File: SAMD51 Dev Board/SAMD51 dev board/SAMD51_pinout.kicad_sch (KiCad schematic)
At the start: 10 parts, among them U1 SAMD51

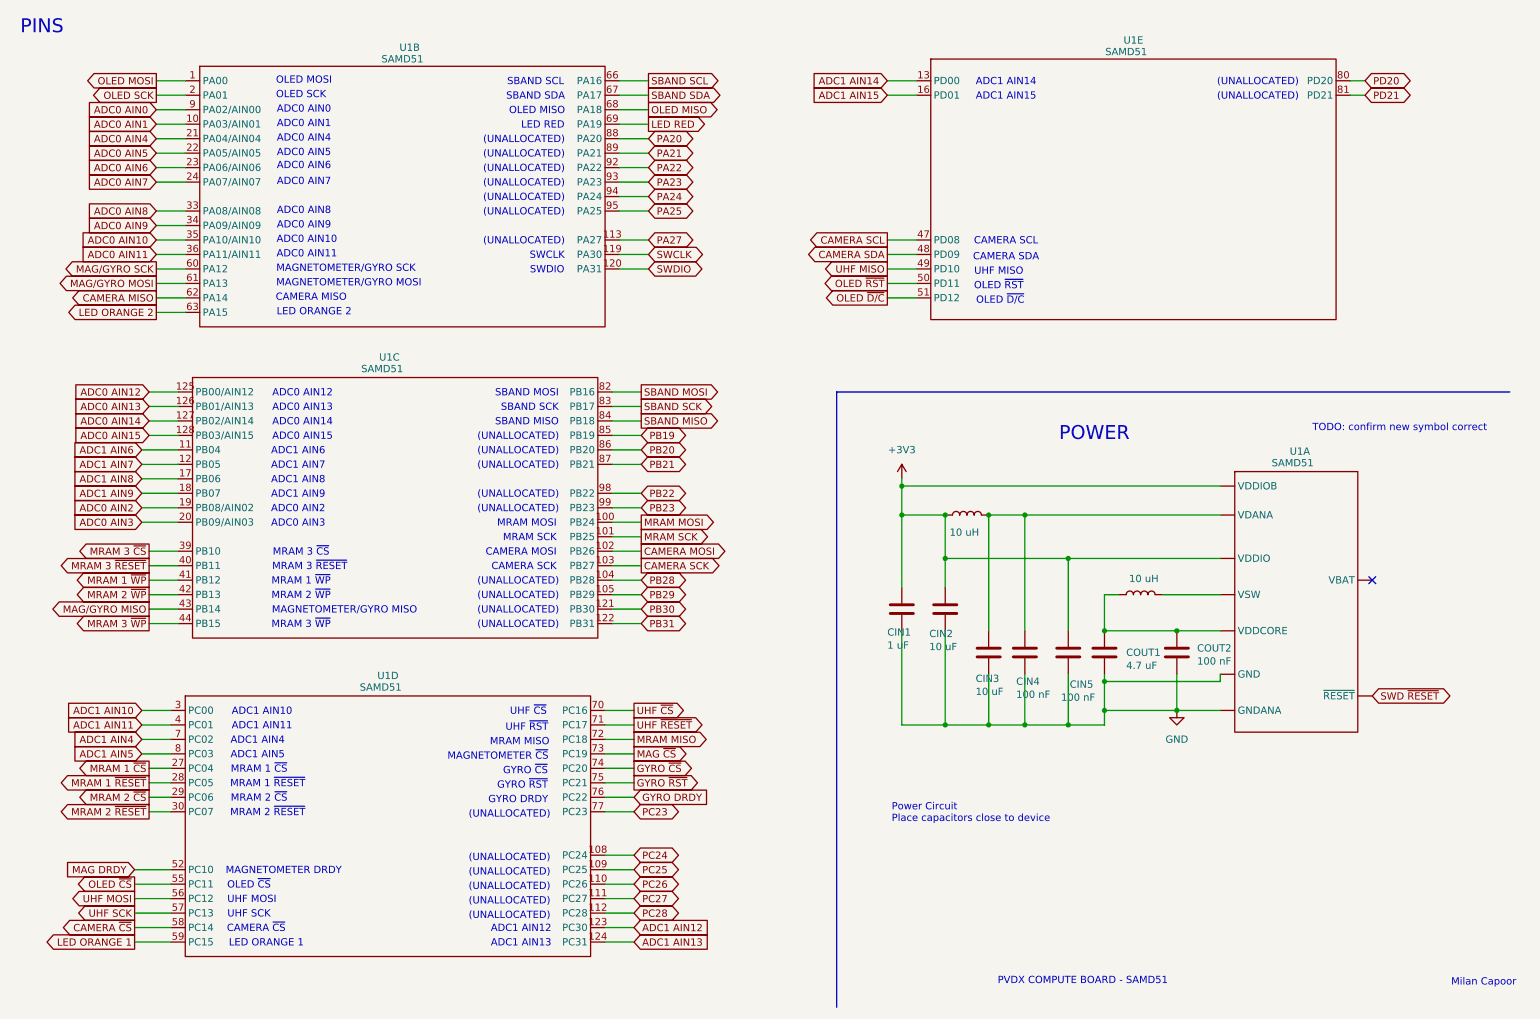
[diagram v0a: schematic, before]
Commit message: routed samd51 breakout
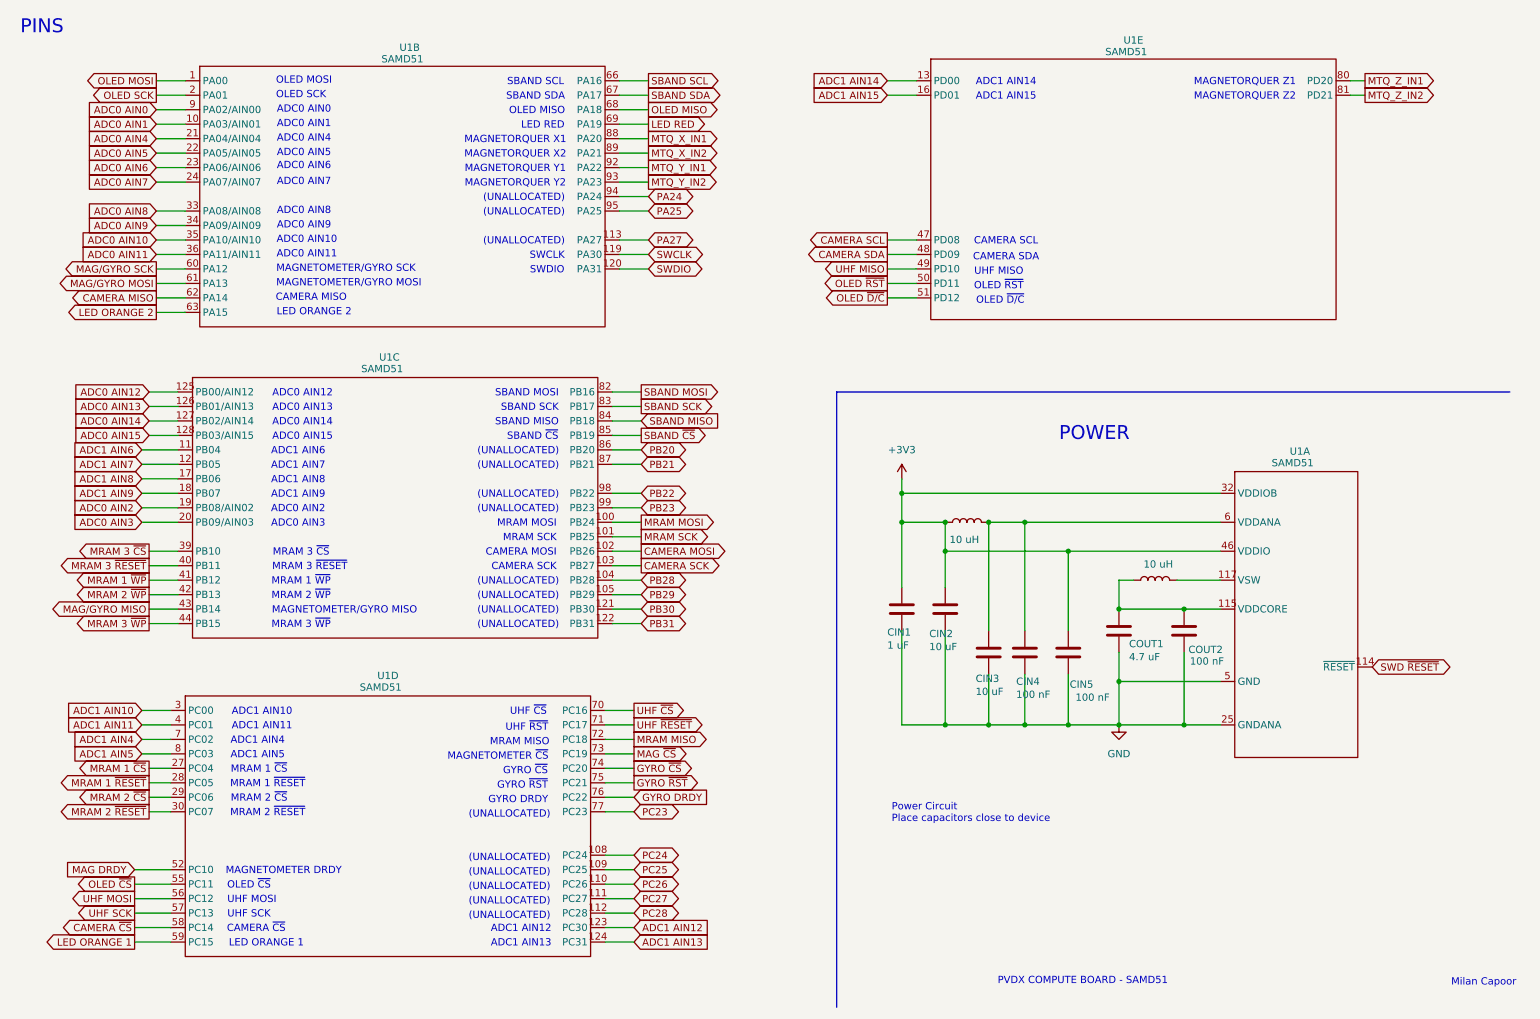
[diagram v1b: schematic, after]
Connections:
- net +3V3: now also U1.107 (VDDIO), U1.118 (VDDIO), U1.32 (VDDIOB), U1.37 (VDDIOB), U1.46 (VDDIO), U1.54 (VDDIO), U1.65 (VDDIO), U1.79 (VDDIO), U1.91 (VDDIO), U1.97 (VDDIO); no longer U1. (~{RESET})
- net GND: now also U1.106 (GND), U1.14 (GNDANA), U1.25 (GNDANA), U1.31 (GND), U1.38 (GND), U1.45 (GND), U1.5 (GND), U1.53 (GND), U1.64 (GND), U1.78 (GND), U1.90 (GND), U1.96 (GND); no longer U1. (~{RESET})
- net SWD ~{RESET}: now also U1.114 (~{RESET}); no longer U1. (~{RESET})
- net at CIN3.1, CIN4.1, L3.2: now also U1.15 (VDDANA), U1.26 (VDDANA), U1.6 (VDDANA); no longer U1. (~{RESET})
- net at COUT1.1, COUT2.1, L4.1: now also U1.115 (VDDCORE); no longer U1. (~{RESET})
- net at L4.2: now also U1.117 (VSW); no longer U1. (~{RESET})
- net PA20 renamed MTQ_X_IN1
- net PA21 renamed MTQ_X_IN2
- net PA22 renamed MTQ_Y_IN1
- net PA23 renamed MTQ_Y_IN2
- net PB19 renamed SBAND ~{CS}
- net PD20 renamed MTQ_Z_IN1
- net PD21 renamed MTQ_Z_IN2
- no-connect marks 1 -> 0
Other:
- note added: "MAGNETORQUER X1"
- note added: "MAGNETORQUER X2"
- note added: "MAGNETORQUER Y1"
- note added: "MAGNETORQUER Y2"
- note added: "MAGNETORQUER Z1"
- note added: "MAGNETORQUER Z2"
- note added: "SBAND ~{CS}"
- note removed: "TODO: confirm new symbol correct"
- moved on the sheet: COUT1, COUT2
